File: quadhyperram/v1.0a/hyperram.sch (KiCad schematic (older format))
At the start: 4 parts, among them U1 S70KL1281

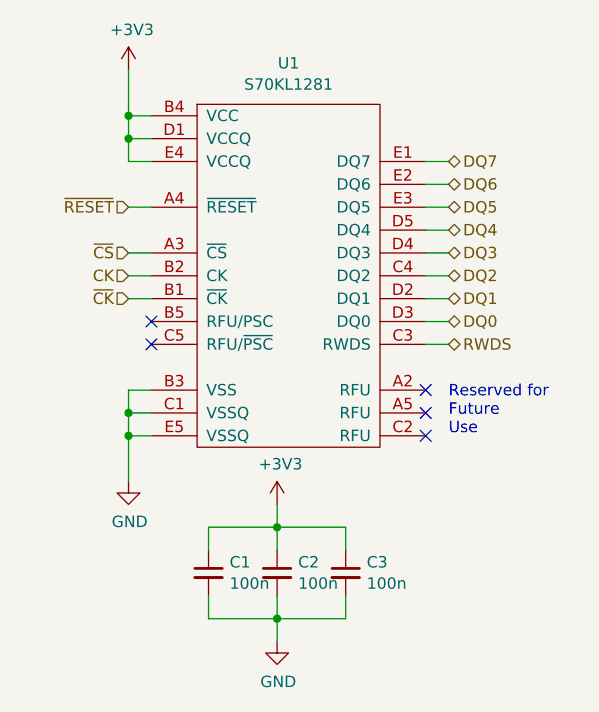
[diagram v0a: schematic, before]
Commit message: Updated quadhyperram Pmod with length matched signals.
Only data, RWDS and Clock signals are length matched. CS is not that
critical and RESET is totally timing irrelevant as far as I know.
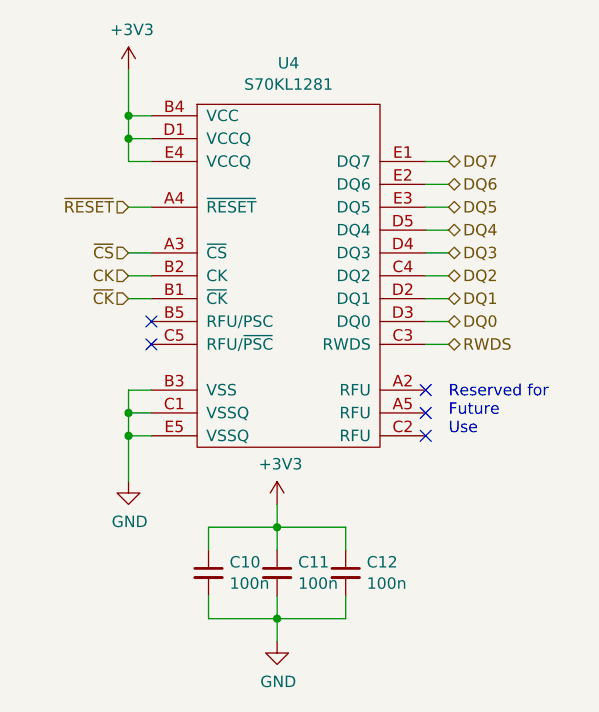
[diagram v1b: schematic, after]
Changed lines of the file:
@@
 $Descr A4 11693 8268
 encoding utf-8
-Sheet 2 5
+Sheet 5 5
 Title "iCEBreaker PMOD - Hyperram"
 Date ""
@@
 AR Path="/5E10E152/5E0FA7AE" Ref="U3"  Part="1"
 AR Path="/5E10E17B/5E0FA7AE" Ref="U4"  Part="1"
-F 0 "U1" H 5600 3680 50  0000 C CNN
+F 0 "U4" H 5600 3680 50  0000 C CNN
 F 1 "S70KL1281" H 5600 3587 50  0000 C CNN
 F 2 "pkl_housings_bga:BGA-24_5x5_6.0x8.0mm" H 6200 1850 50  0001 C CNN
@@
 AR Path="/5E10E152/5E0FA7CA" Ref="#PWR010"  Part="1"
 AR Path="/5E10E17B/5E0FA7CA" Ref="#PWR014"  Part="1"
-F 0 "#PWR02" H 4900 3400 50  0001 C CNN
+F 0 "#PWR014" H 4900 3400 50  0001 C CNN
 F 1 "GND" H 4905 3474 50  0000 C CNN
 F 2 "" H 4900 3650 50  0001 C CNN
@@
 AR Path="/5E10E152/5E0FA7EE" Ref="C7"  Part="1"
 AR Path="/5E10E17B/5E0FA7EE" Ref="C10"  Part="1"
-F 0 "C1" H 5342 4097 50  0000 L CNN
+F 0 "C10" H 5342 4097 50  0000 L CNN
 F 1 "100n" H 5342 4004 50  0000 L CNN
 F 2 "pkl_dipol:C_0402" H 5342 3957 60  0001 L CNN
@@
 AR Path="/5E10E152/5E0FA7F5" Ref="C8"  Part="1"
 AR Path="/5E10E17B/5E0FA7F5" Ref="C11"  Part="1"
-F 0 "C2" H 5642 4097 50  0000 L CNN
+F 0 "C11" H 5642 4097 50  0000 L CNN
 F 1 "100n" H 5642 4004 50  0000 L CNN
 F 2 "pkl_dipol:C_0402" H 5550 4050 60  0001 C CNN
@@
 AR Path="/5E10E152/5E0FA7FC" Ref="C9"  Part="1"
 AR Path="/5E10E17B/5E0FA7FC" Ref="C12"  Part="1"
-F 0 "C3" H 5942 4097 50  0000 L CNN
+F 0 "C12" H 5942 4097 50  0000 L CNN
 F 1 "100n" H 5942 4004 50  0000 L CNN
 F 2 "pkl_dipol:C_0402" H 5850 4050 60  0001 C CNN
@@
 AR Path="/5E10E152/5E0FA810" Ref="#PWR012"  Part="1"
 AR Path="/5E10E17B/5E0FA810" Ref="#PWR016"  Part="1"
-F 0 "#PWR04" H 5550 4100 50  0001 C CNN
+F 0 "#PWR016" H 5550 4100 50  0001 C CNN
 F 1 "GND" H 5555 4174 50  0000 C CNN
 F 2 "" H 5550 4350 50  0001 C CNN
@@
 AR Path="/5E10E152/5E0FA816" Ref="#PWR011"  Part="1"
 AR Path="/5E10E17B/5E0FA816" Ref="#PWR015"  Part="1"
-F 0 "#PWR03" H 5550 3600 50  0001 C CNN
+F 0 "#PWR015" H 5550 3600 50  0001 C CNN
 F 1 "+3V3" H 5565 3926 50  0000 C CNN
 F 2 "" H 5550 3750 50  0001 C CNN
@@
 AR Path="/5E10E152/5E0FA7C4" Ref="#PWR09"  Part="1"
 AR Path="/5E10E17B/5E0FA7C4" Ref="#PWR013"  Part="1"
-F 0 "#PWR01" H 4900 1700 50  0001 C CNN
+F 0 "#PWR013" H 4900 1700 50  0001 C CNN
 F 1 "+3V3" H 4915 2026 50  0000 C CNN
 F 2 "" H 4900 1850 50  0001 C CNN

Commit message: Added optional 1v8 vreg for higher speed S27KS chips.
When using the S27KS chips, the host Pmod IO voltage has to be set to
1.8V too. But as it often is bit of a hassle to change the supply
voltage on the Pmod connector we provide the option of mounting a 1.8V
regulator directly on the Pmod itself to power the chips.
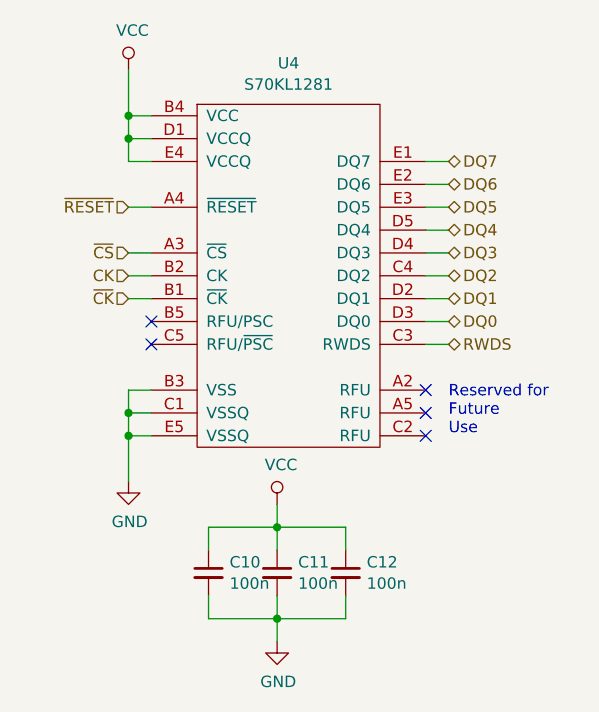
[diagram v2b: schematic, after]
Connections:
- net +3V3 renamed VCC
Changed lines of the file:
@@
 ~CK
 $Comp
-L power:+3V3 #PWR03
-U 1 1 5E0FA816
+L power:VCC #PWR0115
+U 1 1 5E1701E2
+P 4900 1850
+AR Path="/5E0F44B0/5E1701E2" Ref="#PWR0115"  Part="1"
+AR Path="/5E10A443/5E1701E2" Ref="#PWR0117"  Part="1"
+AR Path="/5E10E152/5E1701E2" Ref="#PWR0119"  Part="1"
+AR Path="/5E10E17B/5E1701E2" Ref="#PWR0121"  Part="1"
+F 0 "#PWR0121" H 4900 1700 50  0001 C CNN
+F 1 "VCC" H 4917 2023 50  0000 C CNN
+F 2 "" H 4900 1850 50  0001 C CNN
+F 3 "" H 4900 1850 50  0001 C CNN
+	1    4900 1850
+	1    0    0    -1
+$EndComp
+$Comp
+L power:VCC #PWR0116
+U 1 1 5E1702E5
 P 5550 3750
-AR Path="/5E0F44B0/5E0FA816" Ref="#PWR03"  Part="1"
-AR Path="/5E10A443/5E0FA816" Ref="#PWR07"  Part="1"
-AR Path="/5E10E152/5E0FA816" Ref="#PWR011"  Part="1"
-AR Path="/5E10E17B/5E0FA816" Ref="#PWR015"  Part="1"
-F 0 "#PWR015" H 5550 3600 50  0001 C CNN
-F 1 "+3V3" H 5565 3926 50  0000 C CNN
+AR Path="/5E0F44B0/5E1702E5" Ref="#PWR0116"  Part="1"
+AR Path="/5E10A443/5E1702E5" Ref="#PWR0118"  Part="1"
+AR Path="/5E10E152/5E1702E5" Ref="#PWR0120"  Part="1"
+AR Path="/5E10E17B/5E1702E5" Ref="#PWR0122"  Part="1"
+F 0 "#PWR0122" H 5550 3600 50  0001 C CNN
+F 1 "VCC" H 5567 3923 50  0000 C CNN
 F 2 "" H 5550 3750 50  0001 C CNN
 F 3 "" H 5550 3750 50  0001 C CNN
@@
 	1    0    0    -1
 $EndComp
-$Comp
-L power:+3V3 #PWR01
-U 1 1 5E0FA7C4
-P 4900 1850
-AR Path="/5E0F44B0/5E0FA7C4" Ref="#PWR01"  Part="1"
-AR Path="/5E10A443/5E0FA7C4" Ref="#PWR05"  Part="1"
-AR Path="/5E10E152/5E0FA7C4" Ref="#PWR09"  Part="1"
-AR Path="/5E10E17B/5E0FA7C4" Ref="#PWR013"  Part="1"
-F 0 "#PWR013" H 4900 1700 50  0001 C CNN
-F 1 "+3V3" H 4915 2026 50  0000 C CNN
-F 2 "" H 4900 1850 50  0001 C CNN
-F 3 "" H 4900 1850 50  0001 C CNN
-	1    4900 1850
-	1    0    0    -1
-$EndComp
